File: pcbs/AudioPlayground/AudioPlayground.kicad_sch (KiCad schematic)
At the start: 0 parts

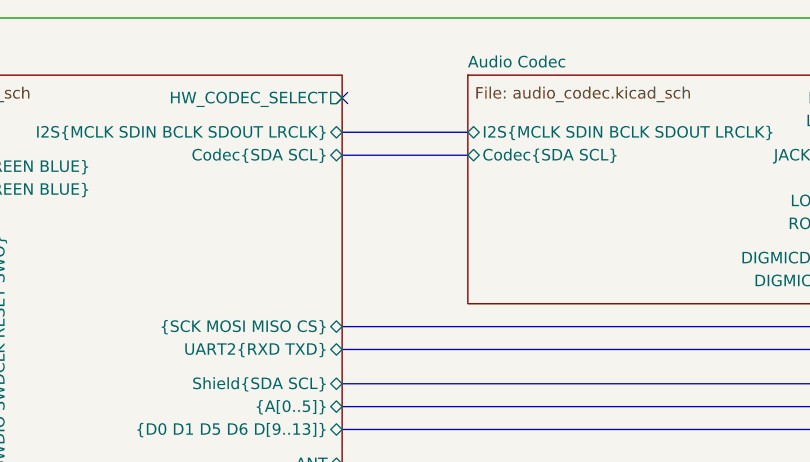
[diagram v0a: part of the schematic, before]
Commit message: Fix Codec IRQ
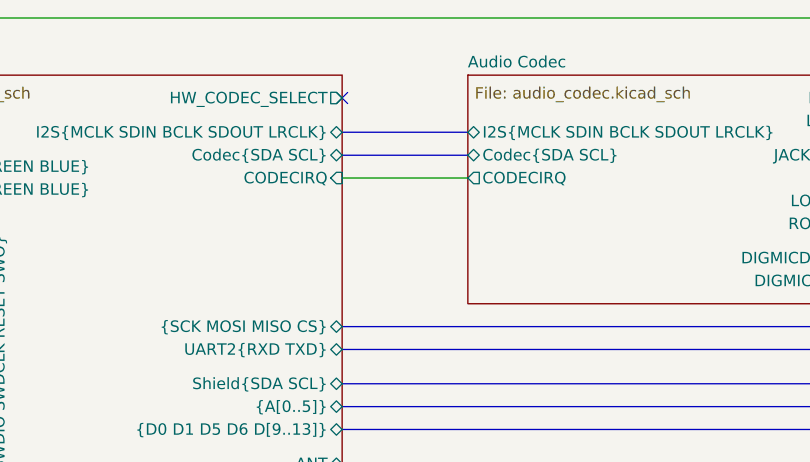
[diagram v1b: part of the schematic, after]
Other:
- sheet Audio Codec ports: added CODECIRQ; removed none
- sheet MCU ports: added CODECIRQ; removed none
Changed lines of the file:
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@@
+	(wire
+		(pts
+			(xy 138.43 59.69) (xy 152.4 59.69)
+		)
+		(stroke
+			(width 0)
+			(type default)
+		)
+	)
 	(wire
 		(pts
@@
 				)
 				(justify left)
+			)
+		)
+		(pin "CODECIRQ" input
+			(at 138.43 59.69 0)
+			(effects
+				(font
+					(size 1.27 1.27)
+				)
+				(justify right)
 			)
 		)
@@
 			)
 		)
+		(pin "CODECIRQ" output
+			(at 152.4 59.69 180)
+			(effects
+				(font
+					(size 1.27 1.27)
+				)
+				(justify left)
+			)
+		)

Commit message: Improve Optic
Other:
- title: BLE Audio Devboard -> LE Audio Playground
